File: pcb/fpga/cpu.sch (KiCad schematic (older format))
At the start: 34 parts

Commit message: fpga pcb power nets
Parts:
- removed L?: L, symbol INDUCTOR_SMALL
- added C?: 10uF, symbol Csmall
- added C?: 0.1uF, symbol Csmall
- added C?: 0.001uF, symbol Csmall
- added C? (x2): 100uF, symbol Csmall
- added C? (x4): 0.01uF, symbol Csmall
- added C? (x2): 10uF, symbol C
- added C? (x10): 0.2uF, symbol Csmall
- added FB? (x2): FILTER, symbol FILTER
- C? (x2): value 10uF -> 1000uF
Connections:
- net labels added: VCCINT, VCCIO, VPLL
- wire segments 129 -> 174
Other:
- moved on the sheet: C?, U?

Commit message: fpga pcb removed configuration device programming header
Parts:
- removed JP?: JUMPER3, symbol JUMPER3
- removed P?: DOWNLOAD, symbol CONN_5X2
- removed R?: 10K, symbol R
- added C?: 10uF, symbol Csmall
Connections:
- net labels removed: ASD, CONF_DONE, DATA, DCLK, ~CE, ~CONFIG, ~CS
- wire segments 174 -> 168
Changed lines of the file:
@@
-$EndComp
-$Comp
-L R R?
-U 1 1 549CABC7
-P 3600 2150
-F 0 "R?" V 3680 2150 40  0000 C CNN
-F 1 "10K" V 3607 2151 40  0000 C CNN
-F 2 "" V 3530 2150 30  0000 C CNN
-F 3 "" H 3600 2150 30  0000 C CNN
-	1    3600 2150
-	-1   0    0    1
 $EndComp
 $Comp
 L GND #PWR?
 U 1 1 549CAC66
-P 3700 1900
-F 0 "#PWR?" H 3700 1900 30  0001 C CNN
-F 1 "GND" H 3700 1830 30  0001 C CNN
-F 2 "" H 3700 1900 60  0000 C CNN
-F 3 "" H 3700 1900 60  0000 C CNN
-	1    3700 1900
-	1    0    0    -1
-$EndComp
-Text GLabel 3600 1700 1    39   Input ~ 0
-~CE
-Text GLabel 3200 2250 1    39   Input ~ 0
-~CONFIG
-Text GLabel 3400 1650 1    39   Input ~ 0
-CONF_DONE
-Text GLabel 3950 900  2    39   Input ~ 0
-DCLK
-Text GLabel 4050 1000 2    39   Input ~ 0
-~CS
-Text GLabel 4150 1100 2    39   Input ~ 0
-ASD
-Text GLabel 3850 800  2    39   Input ~ 0
-DATA
-$Comp
-L CONN_5X2 P?
-U 1 1 549CB4B4
-P 1500 1950
-F 0 "P?" H 1500 2250 60  0000 C CNN
-F 1 "DOWNLOAD" V 1500 1950 50  0000 C CNN
-F 2 "" H 1500 1950 60  0000 C CNN
-F 3 "" H 1500 1950 60  0000 C CNN
-	1    1500 1950
-	1    0    0    -1
-$EndComp
-Text GLabel 1100 1750 0    39   Input ~ 0
-DCLK
-Text GLabel 1900 1750 2    39   Input ~ 0
-CONF_DONE
-Text GLabel 1100 1850 0    39   Input ~ 0
-~CONFIG
-Text GLabel 1900 1850 2    39   Input ~ 0
-DATA
-Text GLabel 1100 1950 0    39   Input ~ 0
-ASD
-Text GLabel 1100 2050 0    39   Input ~ 0
-~CS
-Text GLabel 1900 2050 2    39   Input ~ 0
-~CE
-$Comp
-L GND #PWR?
-U 1 1 549CB76F
-P 2100 2300
-F 0 "#PWR?" H 2100 2300 30  0001 C CNN
-F 1 "GND" H 2100 2230 30  0001 C CNN
-F 2 "" H 2100 2300 60  0000 C CNN
-F 3 "" H 2100 2300 60  0000 C CNN
-	1    2100 2300
-	1    0    0    -1
-$EndComp
-$Comp
-L +3.3V #PWR?
-U 1 1 549CB838
-P 750 2050
-F 0 "#PWR?" H 750 2010 30  0001 C CNN
-F 1 "+3.3V" H 750 2160 30  0000 C CNN
-F 2 "" H 750 2050 60  0000 C CNN
-F 3 "" H 750 2050 60  0000 C CNN
-	1    750  2050
+P 3700 2350
+F 0 "#PWR?" H 3700 2350 30  0001 C CNN
+F 1 "GND" H 3700 2280 30  0001 C CNN
+F 2 "" H 3700 2350 60  0000 C CNN
+F 3 "" H 3700 2350 60  0000 C CNN
+	1    3700 2350
 	1    0    0    -1
 $EndComp
@@
 F 3 "" H 4750 2350 60  0000 C CNN
 	1    4750 2350
-	1    0    0    -1
-$EndComp
-$Comp
-L JUMPER3 JP?
-U 1 1 549CC1A7
-P 4500 2100
-F 0 "JP?" H 4550 2000 40  0000 L CNN
-F 1 "JUMPER3" H 4500 2200 40  0000 C CNN
-F 2 "" H 4500 2100 60  0000 C CNN
-F 3 "" H 4500 2100 60  0000 C CNN
-	1    4500 2100
-	1    0    0    -1
-$EndComp
-$Comp
-L +3.3V #PWR?
-U 1 1 549CC677
-P 4250 1950
-F 0 "#PWR?" H 4250 1910 30  0001 C CNN
-F 1 "+3.3V" H 4250 2060 30  0000 C CNN
-F 2 "" H 4250 1950 60  0000 C CNN
-F 3 "" H 4250 1950 60  0000 C CNN
-	1    4250 1950
 	1    0    0    -1
 $EndComp
@@
 	4100 2450 4100 1100
 Wire Wire Line
-	3400 1100 4150 1100
-Wire Wire Line
-	4000 1000 4000 2450
-Wire Wire Line
-	3400 1000 4050 1000
-Wire Wire Line
 	3900 2450 3900 900
-Wire Wire Line
-	3400 900  3950 900
 Wire Wire Line
 	3800 2450 3800 800
@@
 Connection ~ 6100 7800
 Wire Wire Line
-	2500 1100 2350 1100
+	2150 1100 2500 1100
 Wire Wire Line
 	2350 1100 2350 1300
@@
 Connection ~ 2350 900
 Wire Wire Line
-	2500 800  2350 800
+	2150 800  2500 800
 Connection ~ 2350 800
 Wire Wire Line
@@
 Connection ~ 2700 1750
 Wire Wire Line
-	3200 2250 3200 2450
-Wire Wire Line
 	3300 1950 3300 2450
 Wire Wire Line
 	3300 1950 3200 1950
 Wire Wire Line
-	3400 1650 3400 2450
-Wire Wire Line
 	3400 1750 3200 1750
 Wire Wire Line
-	3600 2450 3600 2400
-Wire Wire Line
-	3600 1700 3600 1900
-Wire Wire Line
-	3600 1800 3700 1800
-Wire Wire Line
-	3700 1800 3700 1900
-Connection ~ 3600 1800
-Connection ~ 3200 2350
-Connection ~ 3400 1750
-Connection ~ 4100 1100
-Connection ~ 4000 1000
-Connection ~ 3900 900
-Wire Wire Line
-	3400 800  3850 800
-Connection ~ 3800 800
-Wire Wire Line
-	1900 1950 2100 1950
-Wire Wire Line
-	2100 1950 2100 2300
-Wire Wire Line
-	1900 2150 2100 2150
-Connection ~ 2100 2150
-Wire Wire Line
-	750  2050 750  2150
-Wire Wire Line
-	750  2150 1100 2150
-Wire Wire Line
 	4600 2450 4600 2250
 Wire Wire Line
-	4600 2250 4750 2250
-Wire Wire Line
-	4750 2100 4750 2350
-Wire Wire Line
-	4500 2200 4500 2450
-Connection ~ 4750 2250
-Wire Wire Line
-	4250 2100 4250 1950
+	4500 2250 4750 2250
 Wire Wire Line
 	7550 1400 7550 2250
@@
 Wire Wire Line
 	9550 2000 9650 2000
+$Comp
+L Csmall C?
+U 1 1 54AB1444
+P 2150 1000
+F 0 "C?" H 2175 1050 30  0000 L CNN
+F 1 "10uF" H 2175 950 30  0000 L CNN
+F 2 "" H 2150 1000 60  0000 C CNN
+F 3 "" H 2150 1000 60  0000 C CNN
+	1    2150 1000
+	1    0    0    -1
+$EndComp
+Connection ~ 2350 1100
+Wire Wire Line
+	2150 900  2150 800
+Wire Wire Line
+	4000 1000 4000 2450
+Wire Wire Line
+	4100 1100 3400 1100
+Wire Wire Line
+	4000 1000 3400 1000
+Wire Wire Line
+	3900 900  3400 900
+Wire Wire Line
+	3800 800  3400 800
+Wire Wire Line
+	3700 2350 3700 2250
+Wire Wire Line
+	3700 2250 3600 2250
+Wire Wire Line
+	3600 2250 3600 2450
+Wire Wire Line
+	3400 1750 3400 2450
+Wire Wire Line
+	3200 2450 3200 2350
+Wire Wire Line
+	4750 2250 4750 2350
+Wire Wire Line
+	4500 2450 4500 2250
+Connection ~ 4600 2250
 $EndSCHEMATC

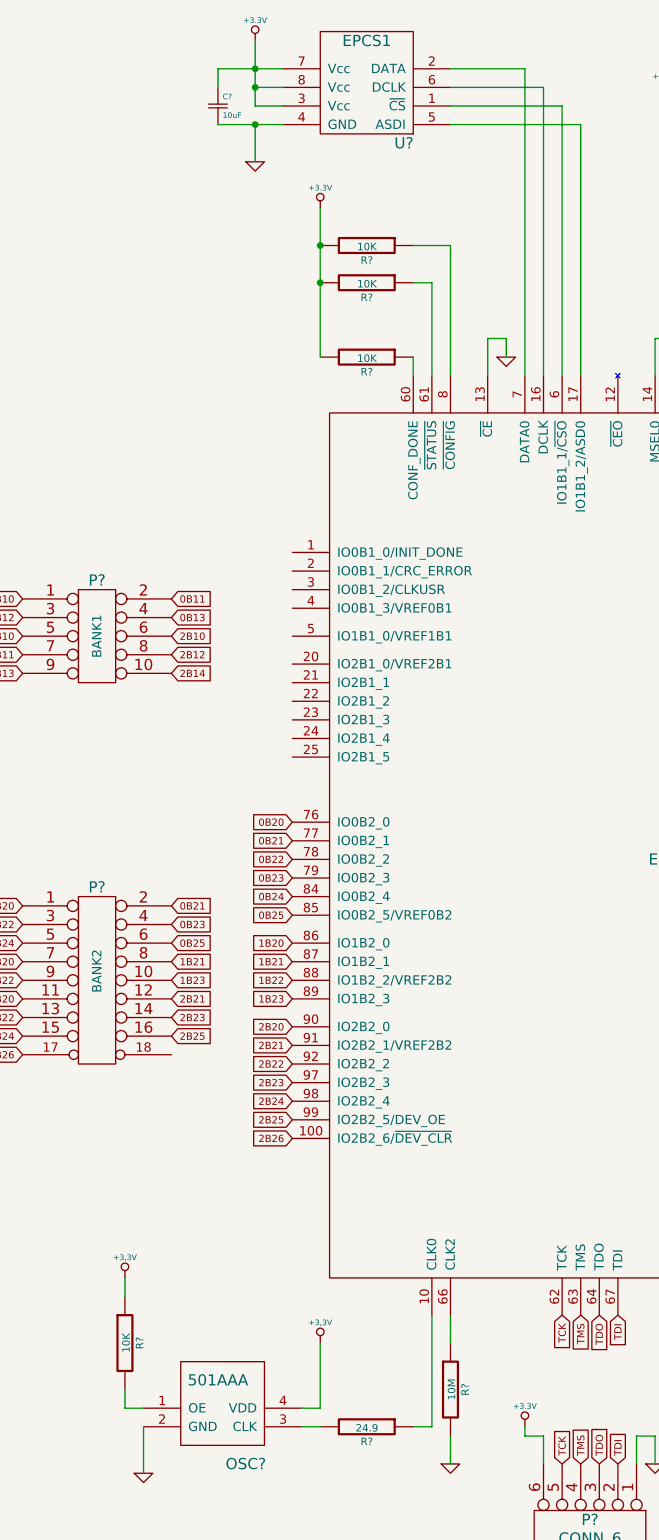
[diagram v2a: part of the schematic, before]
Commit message: fpga pcb - cap on osc vdd
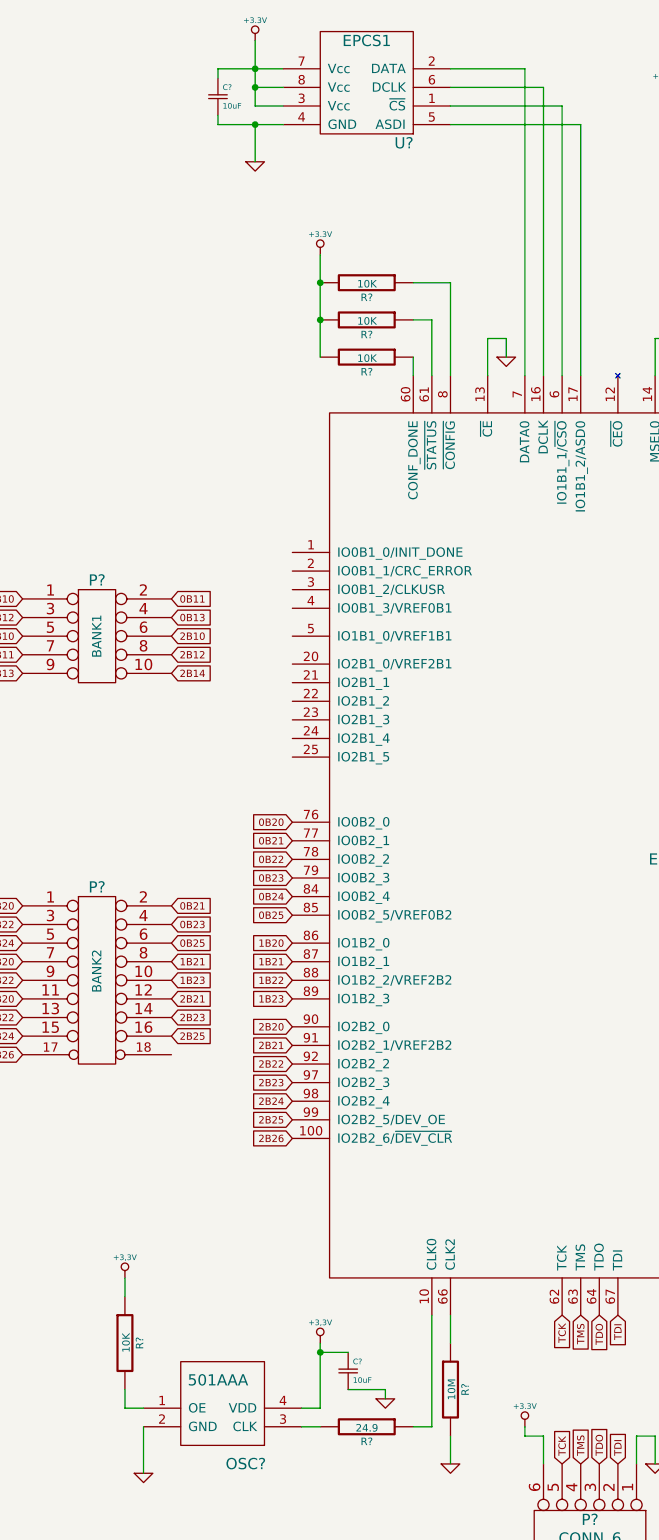
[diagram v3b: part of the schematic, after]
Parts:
- added C?: 10uF, symbol Csmall
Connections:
- net +1.5V: now also C?.1
- net GND: now also C?.2
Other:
- moved on the sheet: C?, R?
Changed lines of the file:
@@
 L R R?
 U 1 1 549CA8C7
+P 2950 2150
+F 0 "R?" V 3030 2150 40  0000 C CNN
+F 1 "10K" V 2957 2151 40  0000 C CNN
+F 2 "" V 2880 2150 30  0000 C CNN
+F 3 "" H 2950 2150 30  0000 C CNN
+	1    2950 2150
+	0    1    1    0
+$EndComp
+$Comp
+L R R?
+U 1 1 549CA925
 P 2950 1950
 F 0 "R?" V 3030 1950 40  0000 C CNN
@@
 $EndComp
 $Comp
-L R R?
-U 1 1 549CA925
-P 2950 1750
-F 0 "R?" V 3030 1750 40  0000 C CNN
-F 1 "10K" V 2957 1751 40  0000 C CNN
-F 2 "" V 2880 1750 30  0000 C CNN
-F 3 "" H 2950 1750 30  0000 C CNN
-	1    2950 1750
-	0    1    1    0
-$EndComp
-$Comp
 L +3.3V #PWR?
 U 1 1 549CA960
-P 2700 1550
-F 0 "#PWR?" H 2700 1510 30  0001 C CNN
-F 1 "+3.3V" H 2700 1660 30  0000 C CNN
-F 2 "" H 2700 1550 60  0000 C CNN
-F 3 "" H 2700 1550 60  0000 C CNN
-	1    2700 1550
+P 2700 1800
+F 0 "#PWR?" H 2700 1760 30  0001 C CNN
+F 1 "+3.3V" H 2700 1910 30  0000 C CNN
+F 2 "" H 2700 1800 60  0000 C CNN
+F 3 "" H 2700 1800 60  0000 C CNN
+	1    2700 1800
 	1    0    0    -1
 $EndComp
@@
 Connection ~ 2350 800
 Wire Wire Line
-	2700 1550 2700 2350
-Connection ~ 2700 1950
-Connection ~ 2700 1750
-Wire Wire Line
-	3300 1950 3300 2450
-Wire Wire Line
-	3300 1950 3200 1950
-Wire Wire Line
-	3400 1750 3200 1750
-Wire Wire Line
 	4600 2450 4600 2250
 Wire Wire Line
@@
 L Csmall C?
 U 1 1 54AB1444
-P 2150 1000
-F 0 "C?" H 2175 1050 30  0000 L CNN
-F 1 "10uF" H 2175 950 30  0000 L CNN
-F 2 "" H 2150 1000 60  0000 C CNN
-F 3 "" H 2150 1000 60  0000 C CNN
-	1    2150 1000
+P 2150 950
+F 0 "C?" H 2175 1000 30  0000 L CNN
+F 1 "10uF" H 2175 900 30  0000 L CNN
+F 2 "" H 2150 950 60  0000 C CNN
+F 3 "" H 2150 950 60  0000 C CNN
+	1    2150 950
 	1    0    0    -1
 $EndComp
 Connection ~ 2350 1100
 Wire Wire Line
-	2150 900  2150 800
-Wire Wire Line
 	4000 1000 4000 2450
 Wire Wire Line
@@
 Wire Wire Line
 	3600 2250 3600 2450
-Wire Wire Line
-	3400 1750 3400 2450
 Wire Wire Line
 	3200 2450 3200 2350
@@
 	4500 2450 4500 2250
 Connection ~ 4600 2250
+Wire Wire Line
+	3200 2150 3300 2150
+Wire Wire Line
+	3300 2150 3300 2450
+Wire Wire Line
+	3400 2450 3400 1950
+Wire Wire Line
+	3400 1950 3200 1950
+Connection ~ 2700 2150
+Connection ~ 2700 1950
+Wire Wire Line
+	2700 1800 2700 2350
+$Comp
+L Csmall C?
+U 1 1 54AB6E81
+P 2850 7800
+F 0 "C?" H 2875 7850 30  0000 L CNN
+F 1 "10uF" H 2875 7750 30  0000 L CNN
+F 2 "" H 2850 7800 60  0000 C CNN
+F 3 "" H 2850 7800 60  0000 C CNN
+	1    2850 7800
+	1    0    0    -1
+$EndComp
+$Comp
+L GND #PWR?
+U 1 1 54AB72AC
+P 3050 7950
+F 0 "#PWR?" H 3050 7950 30  0001 C CNN
+F 1 "GND" H 3050 7880 30  0001 C CNN
+F 2 "" H 3050 7950 60  0000 C CNN
+F 3 "" H 3050 7950 60  0000 C CNN
+	1    3050 7950
+	1    0    0    -1
+$EndComp
+Wire Wire Line
+	2850 7900 3050 7900
+Wire Wire Line
+	3050 7900 3050 7950
+Wire Wire Line
+	2850 7700 2700 7700
+Connection ~ 2700 7700
+Wire Wire Line
+	2150 800  2150 850
+Wire Wire Line
+	2150 1050 2150 1100
 $EndSCHEMATC

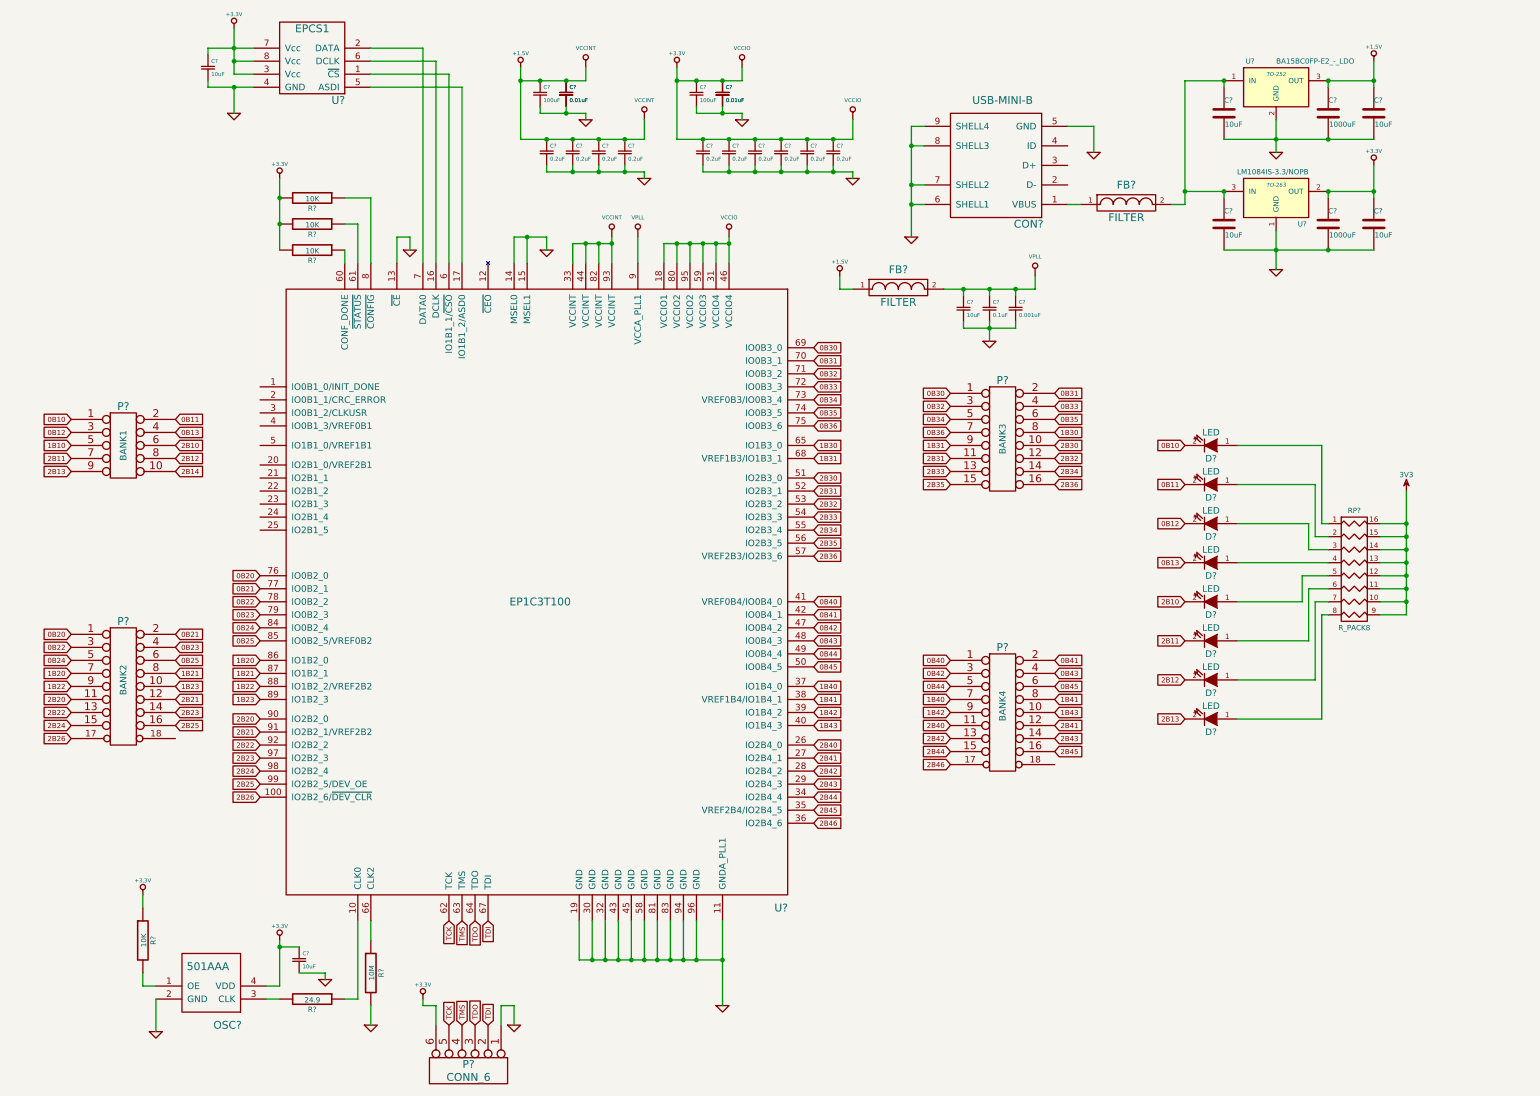
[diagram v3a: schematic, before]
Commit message: fpga pcb - resistor networks
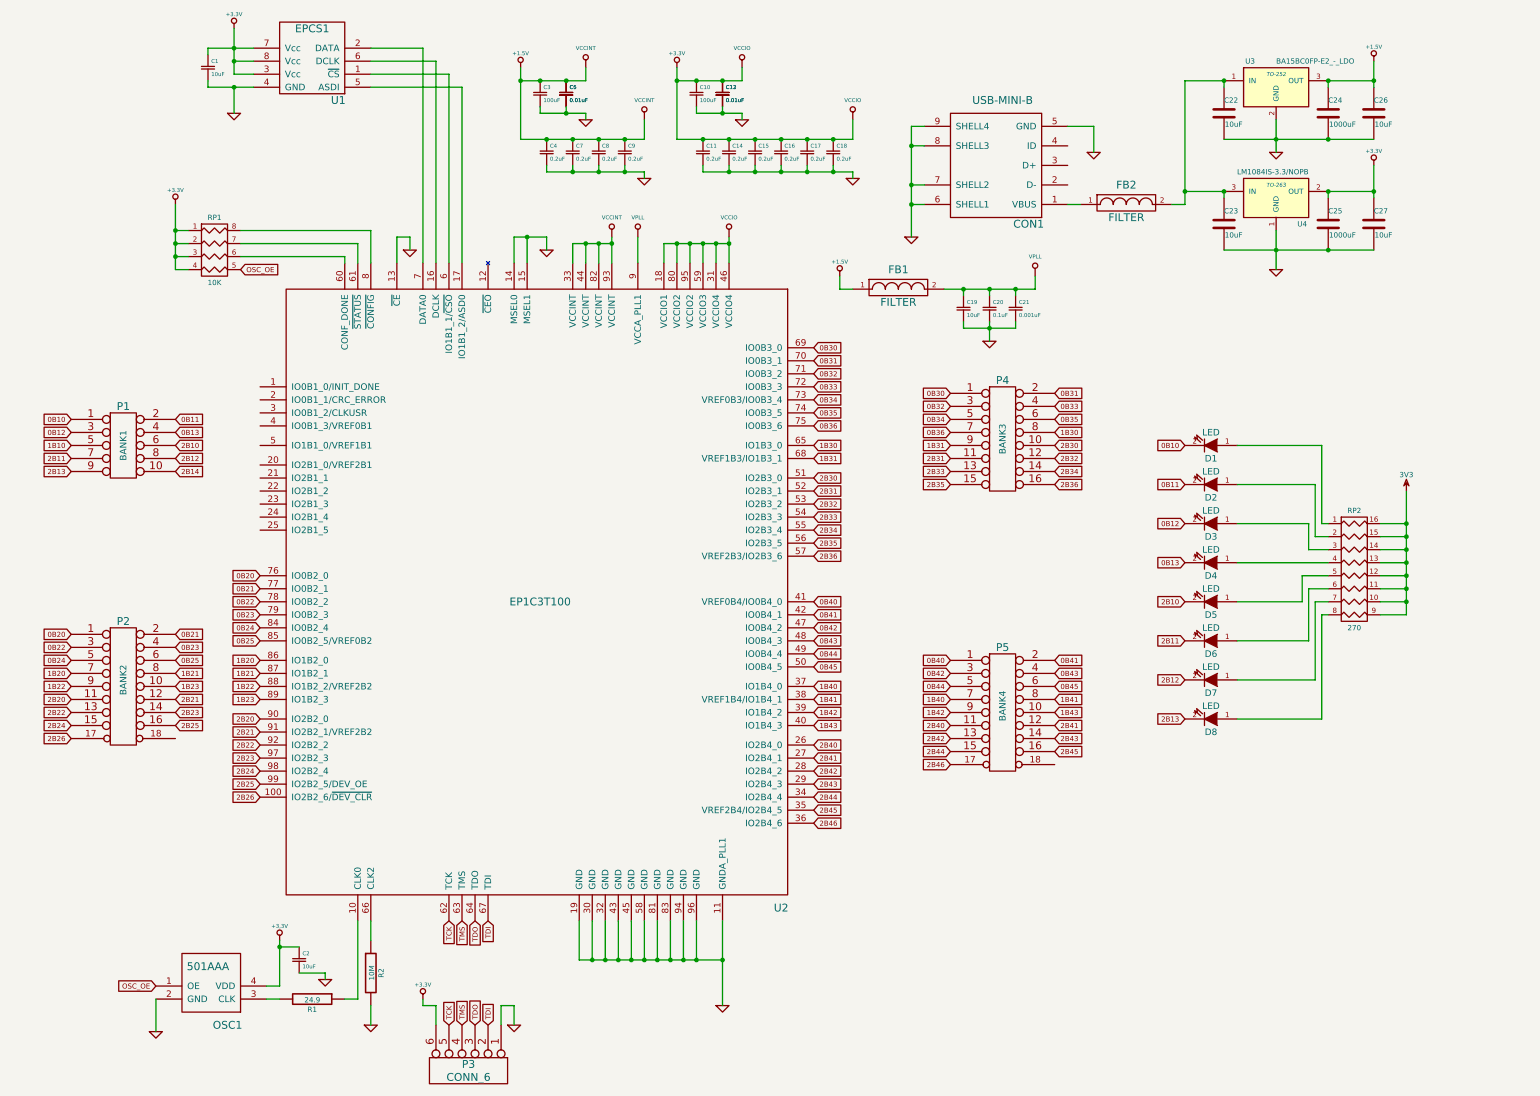
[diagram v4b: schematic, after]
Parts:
- removed R? (x4): 10K, symbol R
- added RP1: 10K, symbol R_PACK4
- RP2: renamed from RP?; value R_PACK8 -> 270
- gave numbers to parts that had none: 50
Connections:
- net +1.5V: now also RP1.1 (P1), RP1.2 (P2), RP1.3 (P3), RP1.4 (P4)
- net at U2.60 (CONF_DONE): now also RP1.6 (R3)
- net at U2.61 (~STATUS): now also RP1.7 (R2)
- net at U2.8 (~CONFIG): now also RP1.8 (R1)
- net OSC_OE: now reaches OSC1.1 (OE)
- net OSC_OE: now also RP1.5 (R4)
